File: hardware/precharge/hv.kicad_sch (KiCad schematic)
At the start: 19 parts

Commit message: Tweaks made during today's meeting
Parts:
- added R?: R, symbol Device:R
- added U?: LM339, symbol Comparator:LM339
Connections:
- net +12V: now also U?.9 (+)
- net GND: now also U?.8 (-)
- net at D?.1 (K), D?.1 (K): now also R?.1; no longer R?.1, U?.10 (-)
- new net: R?.1, R?.2, U?.10 (-)
- no-connect marks 0 -> 1
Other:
- note added: "MAX(V_{batt}/30, 12V) On startup, both voltages we are measuring will be 0. Due to the unknown sign of the comparator's input offset voltage, this could result in a situation where it thinks it's charged when it isn't. The diode here ensures that if the voltage before the precharge resistor is below 360V, the CHARGED signal will be OFF."
- note removed: "MIN(V_{batt}/30, 12V) On startup, both voltages we are measuring will be 0. Due to the unknown sign of the comparator's input offset voltage, this could result in a situation where it thinks it's charged when it isn't. The diode here ensures that if the voltage before the precharge resistor is below 360V, the CHARGED signal will be OFF."
- moved on the sheet: D?, U?E

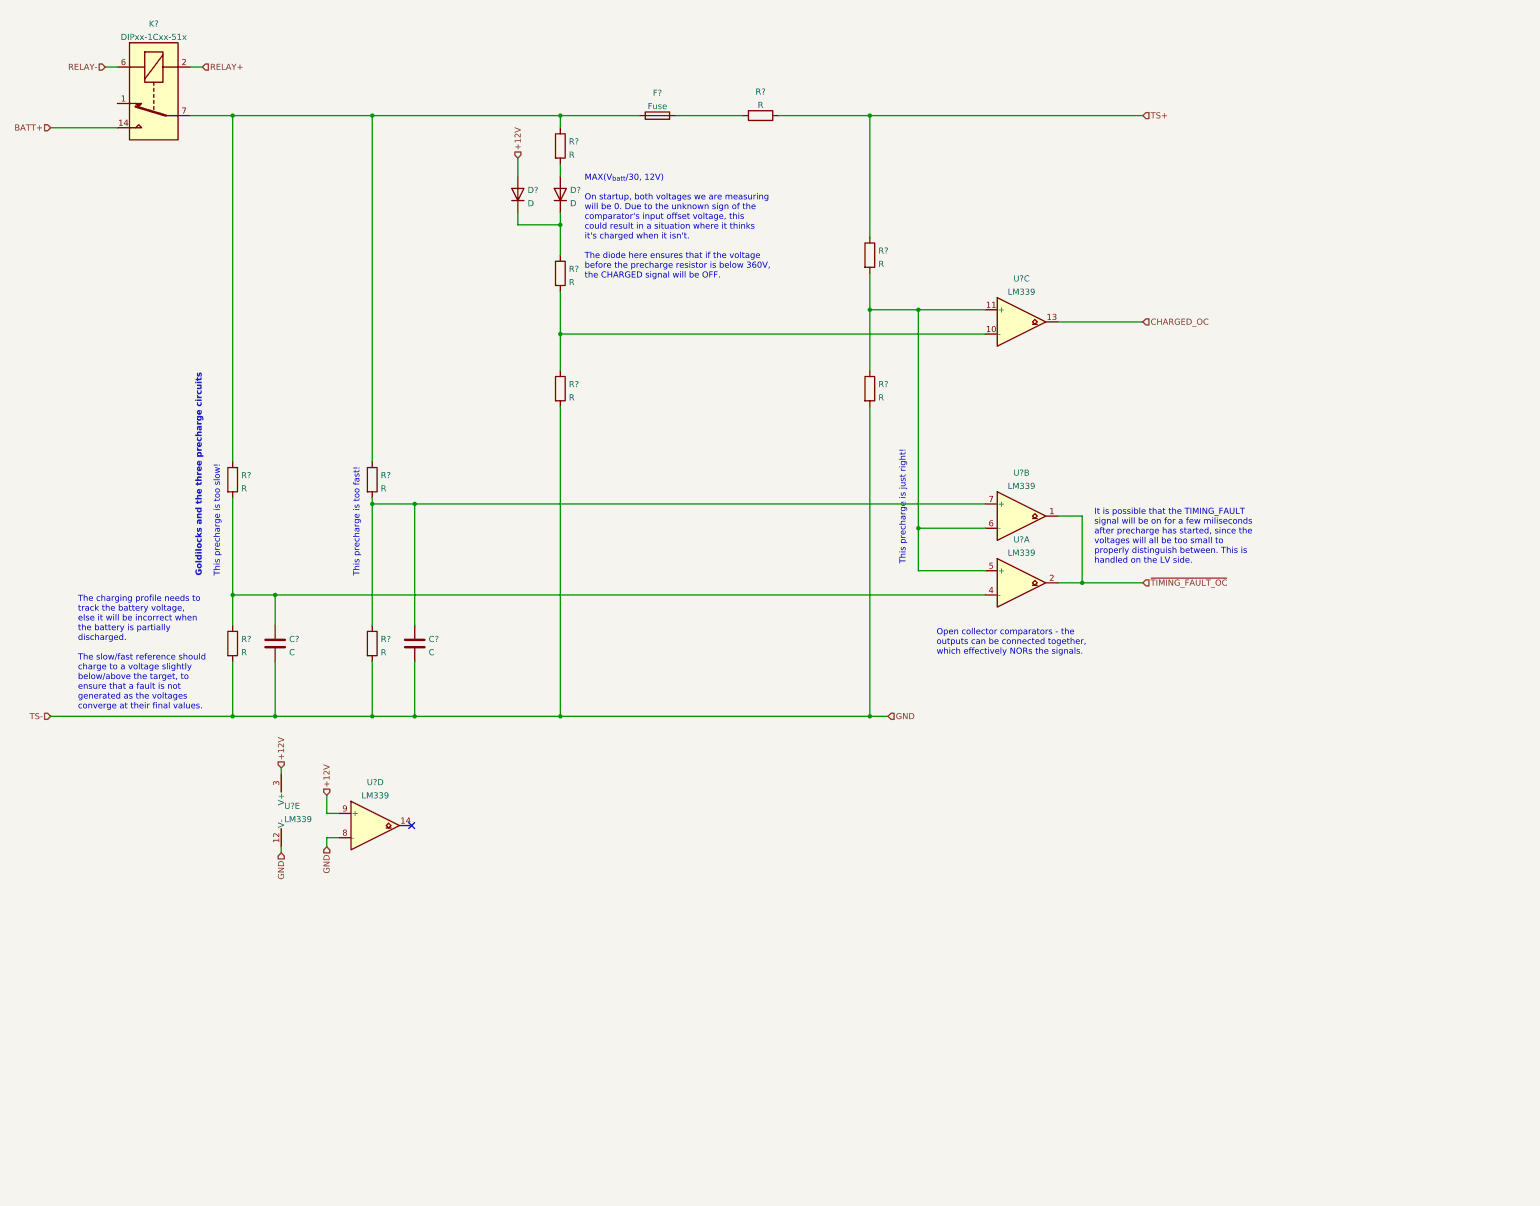
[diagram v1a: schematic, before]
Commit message: Updated quite a bit
- Added relay mechanical state detection

- Selected most component values for HV side

- Other miscellaneous changes
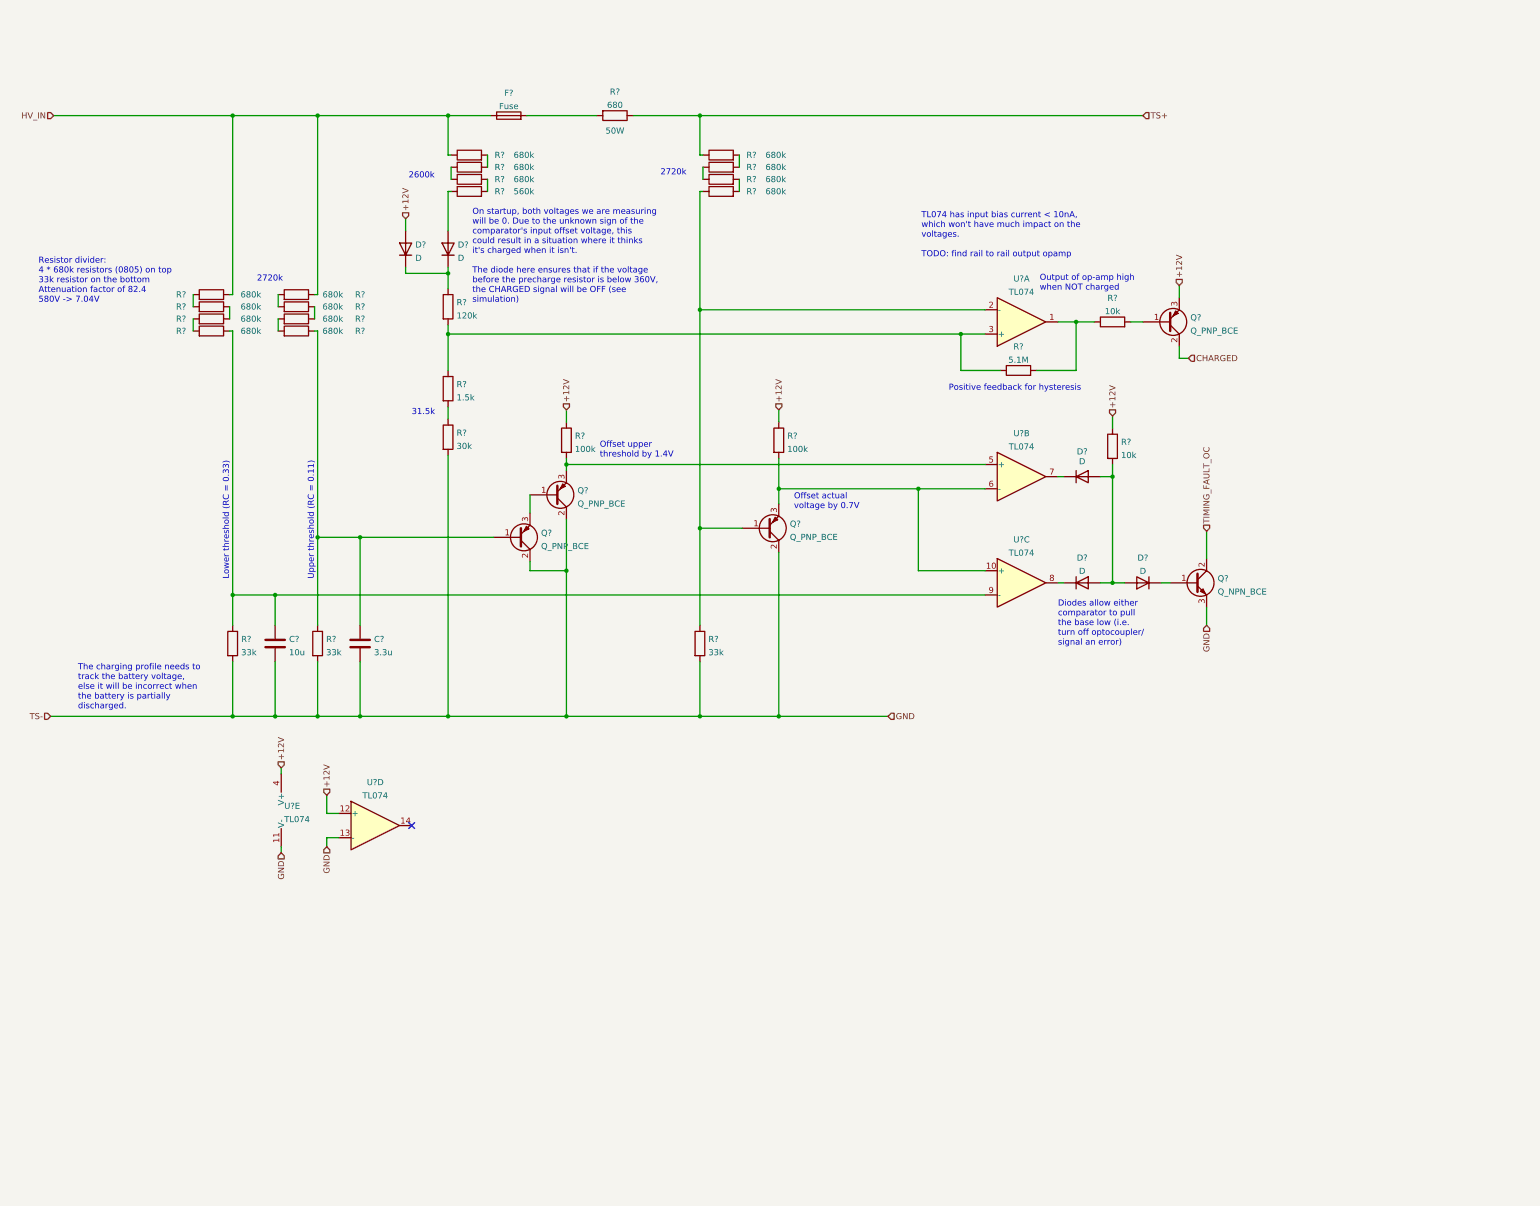
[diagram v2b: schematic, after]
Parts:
- removed K?: DIPxx-1Cxx-51x, Relay_THT:Relay_StandexMeder_DIP_LowProfile, symbol Relay:DIPxx-1Cxx-51x
- removed R? (x3): R, symbol Device:R
- removed U? (x5): LM339, symbol Comparator:LM339
- added D? (x3): D, symbol Device:D
- added Q?: Q_NPN_BCE, symbol Device:Q_NPN_BCE
- added Q? (x4): Q_PNP_BCE, symbol Device:Q_PNP_BCE
- added R? (x14): 680k, symbol Device:R
- added R?: 30k, symbol Device:R
- added R?: 5.1M, symbol Device:R
- added R? (x2): 10k, symbol Device:R
- added R? (x2): 100k, symbol Device:R
- added R?: 560k, symbol Device:R
- added U? (x5): TL074, symbol Amplifier_Operational:TL074
- C?: value C -> 10u
- C?: value C -> 3.3u
- R?: value R -> 680; Power (none) -> 50W
- R?: value R -> 120k
- R? (x3): value R -> 33k
- R?: value R -> 680k
- R?: value R -> 1.5k
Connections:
- net +12V: now also Q?.3 (E), R?.1, R?.1, R?.1, U?.12 (+), U?.4 (V+)
- net GND: now also Q?.2 (C), Q?.2 (C), Q?.2 (C), Q?.3 (E), R?.2, U?.11 (V-), U?.13 (-); no longer R?.2
- net TS+: now also R?.1
- net at R?.1, R?.2: now also R?.1, U?.3 (+)
- net HV_IN: now reaches F?.1, R?.1
- net HV_IN: now also R?.1, R?.1
- net at R?.1: now also Q?.1 (B), R?.1, U?.2 (-)
- net at C?.1, R?.1: now also Q?.1 (B), R?.1
- net at C?.1, R?.1: now also R?.1, U?.9 (-)
- net at D?.2 (A): now also R?.1; no longer R?.2
- new net: D?.1 (K), Q?.1 (B)
- new net: R?.1, R?.1 (x4)
- new net: R?.2, R?.2 (x8)
- new net: R?.1, R?.2
- new net: R?.1, R?.2, U?.1
- new net: Q?.3 (E), R?.2, U?.5 (+)
- new net: Q?.3 (E), R?.2, U?.10 (+), U?.6 (-)
- new net: D?.1 (K), U?.7
- new net: Q?.1 (B), Q?.3 (E)
- new net: Q?.1 (B), R?.2
- new net: D?.2 (A), D?.2 (A), D?.2 (A), R?.2
- new net: D?.1 (K), U?.8
- new net CHARGED: Q?.2 (C)
- new net TIMING_FAULT_OC: Q?.2 (C)
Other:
- note added: "2600k"
- note added: "2720k"
- note added: "31.5k"
- note added: "Diodes allow either comparator to pull the base low (i.e. turn off optocoupler/ signal an error)"
- note added: "Lower threshold (RC = 0.33)"
- note added: "Offset actual voltage by 0.7V"
- note added: "Offset upper threshold by 1.4V"
- note added: "On startup, both voltages we are measuring will be 0. Due to the unknown sign of the comparator's input offset voltage, this could result in a situation where it thinks it's charged when it isn't. The diode here ensures that if the voltage before the precharge resistor is below 360V, the CHARGED signal will be OFF (see simulation)"
- note added: "Output of op-amp high when NOT charged"
- note added: "Positive feedback for hysteresis"
- note added: "Resistor divider: 4 * 680k resistors (0805) on top 33k resistor on the bottom Attenuation factor of 82.4 580V -> 7.04V"
- note added: "TL074 has input bias current < 10nA, which won't have much impact on the voltages. TODO: find rail to rail output opamp"
- note added: "The charging profile needs to track the battery voltage, else it will be incorrect when the battery is partially discharged."
- note added: "Upper threshold (RC = 0.11)"
- note removed: "Goldilocks and the three precharge circuits"
- note removed: "It is possible that the TIMING_FAULT signal will be on for a few miliseconds after precharge has started, since the voltages will all be too small to properly distinguish between. This is handled on the LV side."
- note removed: "MAX(V_{batt}/30, 12V) On startup, both voltages we are measuring will be 0. Due to the unknown sign of the comparator's input offset voltage, this could result in a situation where it thinks it's charged when it isn't. The diode here ensures that if the voltage before the precharge resistor is below 360V, the CHARGED signal will be OFF."
- note removed: "Open collector comparators - the outputs can be connected together, which effectively NORs the signals."
- note removed: "The charging profile needs to track the battery voltage, else it will be incorrect when the battery is partially discharged. The slow/fast reference should charge to a voltage slightly below/above the target, to ensure that a fault is not generated as the voltages converge at their final values."
- note removed: "This precharge is just right!"
- note removed: "This precharge is too fast!"
- note removed: "This precharge is too slow!"
- moved on the sheet: C?, D?, F?, R?

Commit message: Added part numbers for most components, added LEDs, tweaked LV side.
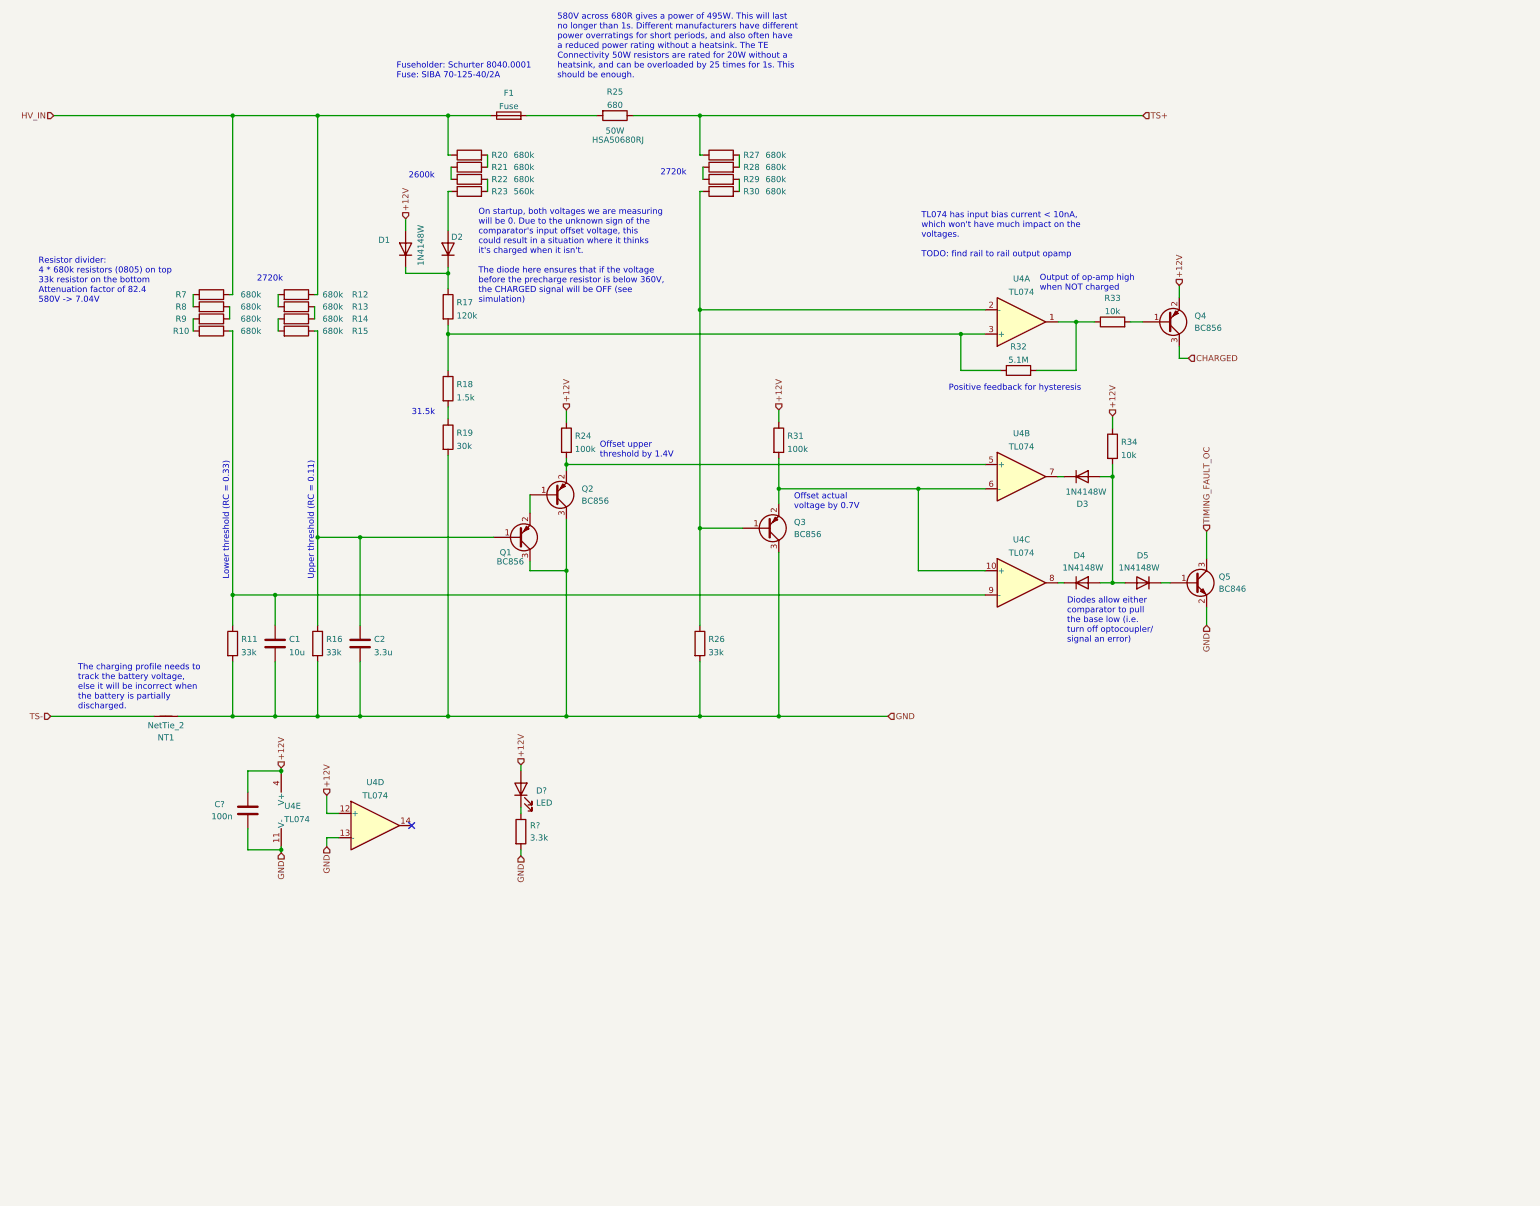
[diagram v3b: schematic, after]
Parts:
- removed D? (x5): D, symbol Device:D
- removed Q?: Q_NPN_BCE, symbol Device:Q_NPN_BCE
- removed Q? (x4): Q_PNP_BCE, symbol Device:Q_PNP_BCE
- added C?: 100n, symbol Device:C
- added D1, D2, D3, D4, D5: 1N4148W, Diode_SMD:D_SOD-123, symbol Diode:1N4148W
- added D?: LED, symbol Device:LED
- added NT1: NetTie_2, symbol Device:NetTie_2
- added Q1, Q2, Q3, Q4: BC856, Package_TO_SOT_SMD:SOT-23, symbol Transistor_BJT:BC856
- added Q5: BC846, Package_TO_SOT_SMD:SOT-23, symbol Transistor_BJT:BC846
- added R?: 3.3k, symbol Device:R
- R25: renamed from R?; MPN (none) -> HSA50680RJ
- gave numbers to parts that had none: 31
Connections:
- net +12V: now also C?.1, D1.2 (A), D?.2 (A), Q4.2 (E)
- net CHARGED: now also Q4.3 (C)
- net GND: now also C?.2, NT1.1, Q1.3 (C), Q2.3 (C), Q3.3 (C), Q5.2 (E), R?.2
- net TIMING_FAULT_OC: now also Q5.3 (C)
- net at R17.1: now also D1.1 (K), D2.1 (K)
- net at C2.1, R15.1, R16.1: now also Q1.1 (B)
- net at R24.2, U4.5 (+): now also Q2.2 (E)
- net at R31.2, U4.10 (+), U4.6 (-): now also Q3.2 (E)
- net at U4.7: now also D3.1 (K)
- net at R33.2: now also Q4.1 (B)
- net at R34.2: now also D3.2 (A), D4.2 (A), D5.2 (A)
- net at R26.1, R30.1, U4.2 (-): now also Q3.1 (B)
- net at R23.1: now also D2.2 (A)
- net at U4.8: now also D4.1 (K)
- new net: Q1.2 (E), Q2.1 (B)
- new net: D5.1 (K), Q5.1 (B)
- new net: D?.1 (K), R?.1
- new net TS-: NT1.2
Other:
- note added: "580V across 680R gives a power of 495W. This will last no longer than 1s. Different manufacturers have different power overratings for short periods, and also often have a reduced power rating without a heatsink. The TE Connectivity 50W resistors are rated for 20W without a heatsink, and can be overloaded by 25 times for 1s. This should be enough."
- note added: "Fuseholder: Schurter 8040.0001 Fuse: SIBA 70-125-40/2A"

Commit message: Tweaks, nearly done
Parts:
- removed D1, D2, D3, D4, D5: 1N4148W, Diode_SMD:D_SOD-123, symbol Diode:1N4148W
- removed Q4: BC856, Package_TO_SOT_SMD:SOT-23, symbol Transistor_BJT:BC856
- removed Q5: BC846, Package_TO_SOT_SMD:SOT-23, symbol Transistor_BJT:BC846
- removed R33, R34: 10k, symbol Device:R
- removed U4: TL074, symbol Amplifier_Operational:TL074
- added D? (x4): BAT54W, Package_TO_SOT_SMD:SOT-323_SC-70, symbol Diode:BAT54W
- added U? (x5): TLV274, symbol Amplifier_Operational:TLC274
- gave numbers to parts that had none: 3
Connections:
- net +12V: now also D?.1 (A), U?.12 (+), U?.4 (V+)
- net GND: now also U?.11 (V-), U?.13 (-)
- net at R17.1: now also D?.3 (K), D?.3 (K)
- net at R17.2, R18.1, R32.1: now also U?.3 (+)
- net at R23.1: now also D?.1 (A)
- net ~{CHARGED}: now reaches R32.2
- net ~{CHARGED}: now also U?.1
- net at Q2.2 (E), R24.2: now also U?.5 (+)
- net at Q3.2 (E), R31.2: now also U?.10 (+), U?.6 (-)
- net at Q3.1 (B), R26.1, R30.1: now also U?.2 (-)
- net at C1.1, R10.1, R11.1: now also U?.9 (-)
- new net: D?.3 (K), U?.7
- new net: D?.3 (K), U?.8
- new net ~{TIMING_FAULT_OC}: D?.1 (A), D?.1 (A)
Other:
- note added: "Diodes allow either comparator to pull the output low (i.e. turn off optocoupler / signal an error). The optocoupler diode voltage drop is > 0.8V, and the BAT54W voltage drop at 12mA is < 0.5V, so the optocoupler will definitely turn off."
- note added: "TLV274 has input bias current < 1nA, which won't have much impact on the voltages, and rail-to-rail outputs that can handle 100mA."
- note removed: "Diodes allow either comparator to pull the base low (i.e. turn off optocoupler/ signal an error)"
- note removed: "Output of op-amp high when NOT charged"
- note removed: "TL074 has input bias current < 10nA, which won't have much impact on the voltages. TODO: find rail to rail output opamp"

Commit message: Assigned some footprints, created footprint library
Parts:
- C1, C2: footprint (none) -> Capacitor_SMD:C_0805_2012Metric
- C12: footprint (none) -> Capacitor_SMD:C_0603_1608Metric
- D13: footprint (none) -> LED_SMD:LED_0603_1608Metric
- NT1: footprint (none) -> NetTie:NetTie-2_SMD_Pad0.5mm
- R10, R12, R13, R14, R15, R20, R21, R22, R23, R27, R28, R29, R30, R7, R8, R9: footprint (none) -> Resistor_SMD:R_0805_2012Metric
- R11, R16, R17, R18, R19, R24, R26, R31, R32, R45: footprint (none) -> Resistor_SMD:R_0603_1608Metric
- R25: footprint (none) -> Resistor_THT:R_Axial_Power_L75.0mm_W9.0mm_P86.36mm
- U4: renamed from U?; footprint (none) -> Package_SO:SOIC-14_3.9x8.7mm_P1.27mm
- gave numbers to parts that had none: 4
